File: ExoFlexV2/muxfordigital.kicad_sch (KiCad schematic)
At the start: 31 parts, among them U100 SN74LVC3G14DCUT_V2, U101 SN74LVC3G14DCUT_V2, U102 SN74LVC1G08DBVR, U103 SN74LVC3G14DCUT_V2, U104 SN74LVC3G14DCUT_V2, U105 SN74LVC3G14DCUT_V2, U106 SN74LVC3G14DCUT_V2, U107 SN74LVC1G32DBVR, U112 SN74LVC1G32DBVR, U113 SN74LVC1G32DBVR, U97 SN74LVC1G08DBVR, U98 SN74LVC1G08DBVR, U99 SN74LVC1G08DBVR

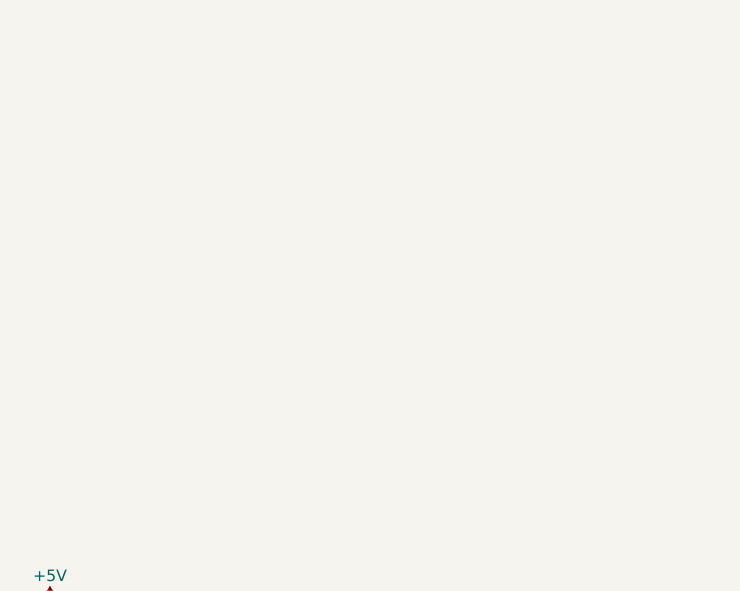
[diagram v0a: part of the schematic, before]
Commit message: Finalisation 1
- Ajout de pages pour la gestion des signaux négatif
- Modification des pages de torque et amplitude
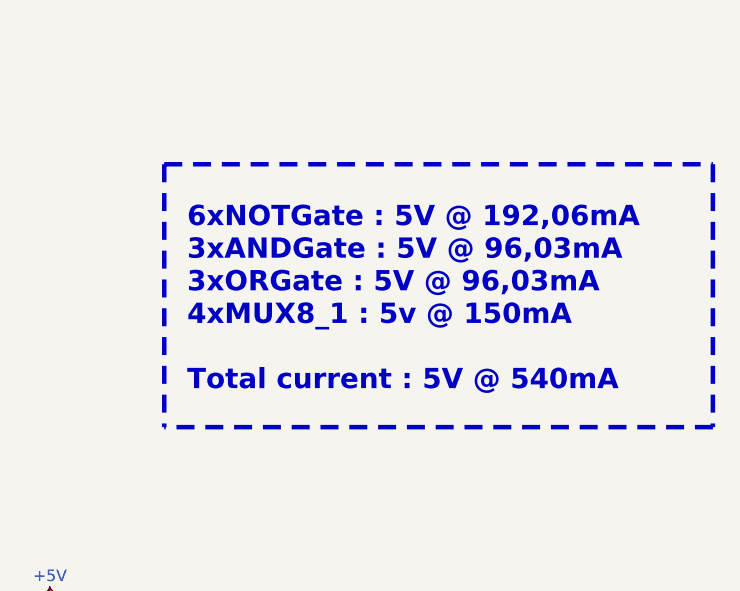
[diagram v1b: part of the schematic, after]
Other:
- note added: "6xNOTGate : 5V @ 192,06mA 3xANDGate : 5V @ 96,03mA 3xORGate : 5V @ 96,03mA 4xMUX8_1 : 5v @ 150mA Total current : 5V @ 540mA"
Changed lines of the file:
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@@
     (stroke (width 0) (type default) (color 0 0 0 0))
+  )
+  (polyline (pts (xy 220.98 34.29) (xy 281.94 34.29))
+    (stroke (width 0.5) (type dash) (color 255 148 44 1))
   )
   (wire (pts (xy 115.57 81.28) (xy 115.57 121.92))
@@
     (stroke (width 0) (type default) (color 0 0 0 0))
   )
+  (polyline (pts (xy 281.94 34.29) (xy 281.94 63.5))
+    (stroke (width 0.5) (type dash) (color 255 148 44 1))
+  )
   (wire (pts (xy 93.98 73.66) (xy 137.16 73.66))
     (stroke (width 0) (type default) (color 0 0 0 0))
@@
     (stroke (width 0) (type default) (color 0 0 0 0))
   )
+  (polyline (pts (xy 281.94 63.5) (xy 220.98 63.5))
+    (stroke (width 0.5) (type dash) (color 255 148 44 1))
+  )
   (wire (pts (xy 242.57 128.27) (xy 234.95 128.27))
     (stroke (width 0) (type default) (color 0 0 0 0))
@@
     (stroke (width 0) (type default) (color 0 0 0 0))
   )
+  (polyline (pts (xy 220.98 34.29) (xy 220.98 63.5))
+    (stroke (width 0.5) (type dash) (color 255 148 44 1))
+  )
   (wire (pts (xy 219.71 85.09) (xy 212.09 85.09))
     (stroke (width 0) (type default) (color 0 0 0 0))
@@
     (stroke (width 0) (type default) (color 0 0 0 0))
   )
+  (text "6xNOTGate : 5V @ 192,06mA\n3xANDGate : 5V @ 96,03mA\n3xORGate : 5V @ 96,03mA\n4xMUX8_1 : 5v @ 150mA\n\nTotal current : 5V @ 540mA"
+    (at 223.52 59.69 0)
+    (effects (font (size 2.25 2.25) (thickness 0.5) bold) (justify left bottom))
+  )
   (global_label "M_LC_POS1_INT" (shape input) (at 137.16 101.6 180) (fields_autoplaced)
